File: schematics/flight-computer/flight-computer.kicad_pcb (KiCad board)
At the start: 4 copper layers, 80 x 80 mm, 114 parts, among them J101 BATT, J102 CHG, J103 Expansion Slot, J104 SWD, J105 BLACKBOX, J106 USB C, J107 GPS, J108 TELEM, J301 BMI-S-201, Q401 Si9933CDY, Q402 BSS138, U101 MAX14787E, U102 STM32F405RGT6, U201 NVT2006BQ, U202 PCA9306, U203 ICM-20789, U204 MS5611-01BA, U301 Si4463, U302 MAX-M8Q, U401 BQ29200, U402 LTC4002-ES8, U403 MAX604, U404 MAX604, Y101 26M, Y301 LFTCXO068373

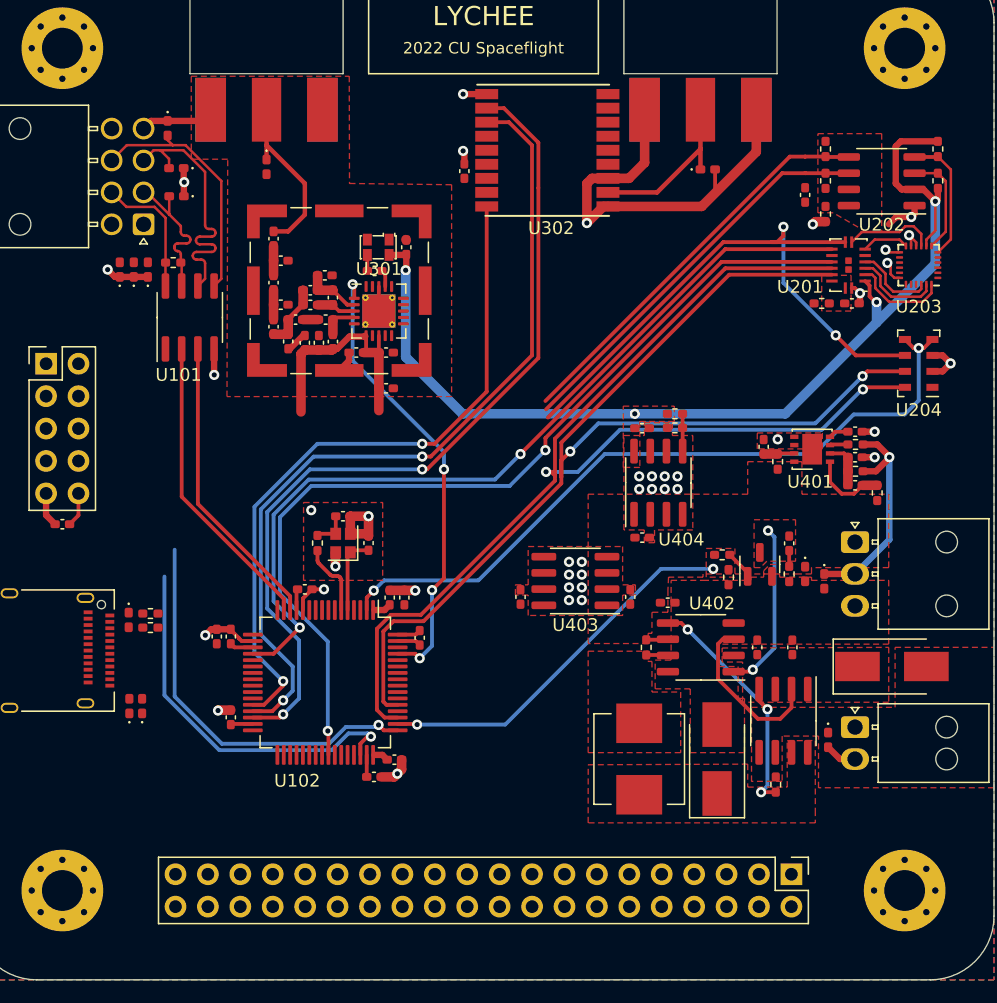
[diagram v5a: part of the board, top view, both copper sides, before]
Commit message: Change peripheral interface assignments to match layout
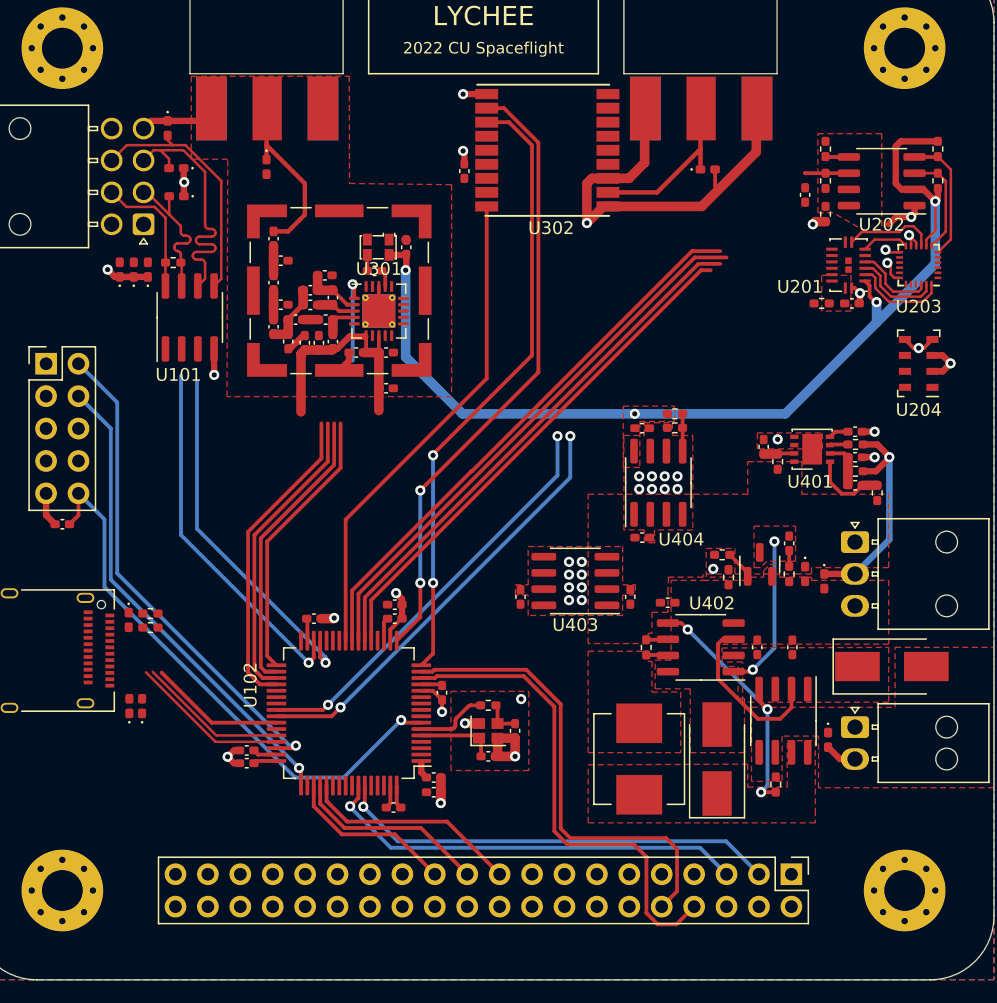
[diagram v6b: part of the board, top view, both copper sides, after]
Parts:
- moved J107 34.1 mm to (225.8, 109.8)
- moved J108 34.0 mm to (191.8, 109.8)
- moved C104 21.6 mm to (211.2, 158.6), turned to 90 degrees
- moved C103 19.2 mm to (209.1, 160.6), turned to 180 degrees
- moved Y101 18.6 mm to (209.1, 158.6), turned to 0 degrees
- moved R102 18.5 mm to (209.1, 156.6), turned to 180 degrees
- moved C106 15.4 mm to (204.8, 163.4), turned to 180 degrees
- moved C105 14.5 mm to (204.8, 162.2), turned to 180 degrees
- moved C108 14.2 mm to (201.8, 148.7), turned to 180 degrees
- moved C107 13.5 mm to (205.4, 155.6), turned to 90 degrees
- moved C112 13.5 mm to (201.7, 164.6), turned to 0 degrees
- moved C101 12.9 mm to (201.8, 149.8), turned to 180 degrees
- moved C102 11.6 mm to (190.2, 161.1), turned to 0 degrees
- moved C110 10.2 mm to (190.2, 160.1), turned to 0 degrees
- moved C109 10.1 mm to (195.4, 149.8), turned to 180 degrees
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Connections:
- J103 pad 10: /EXT_RX -> /UART4_RX
- J103 pad 19: /SPI1_MOSI -> /SPI3_MOSI
- J103 pad 21: /SPI1_MISO -> /SPI3_MISO
- J103 pad 23: /SPI1_SCLK -> /SPI3_SCLK
- J103 pad 3: /EXT_SDA -> /I2C1_SDA
- J103 pad 5: /EXT_SCL -> /I2C1_SCL
- J103 pad 8: /EXT_TX -> /UART4_TX
- R201 pad 2: /IMU_PR_CL -> /I2C3_SCL
- R202 pad 2: /IMU_PR_DA -> /I2C3_SDA
- U101 pad 2: /UART4_RX -> /USART3_RX
- U101 pad 3: /UART4_TX -> /USART3_TX
- U102 pad 16: unconnected-(U102-Pad16) -> /USART2_TX
- U102 pad 17: unconnected-(U102-Pad17) -> /USART2_RX
- U102 pad 20: /IMU_INT -> unconnected-(U102-Pad20)
- U102 pad 24: unconnected-(U102-Pad24) -> /IMU_INT
- U102 pad 25: unconnected-(U102-Pad25) -> /GPS_~{RESET}
- U102 pad 28: /GPS_~{RESET} -> unconnected-(U102-Pad28)
- U102 pad 40: unconnected-(U102-Pad40) -> /I2C3_SDA
- U102 pad 41: /IMU_~{CS} -> /I2C3_SCL
- U102 pad 43: unconnected-(U102-Pad43) -> /IMU_~{CS}
- U102 pad 58: /IMU_PR_CL -> /I2C1_SCL
- U102 pad 59: /IMU_PR_DA -> /I2C1_SDA
- U201 pad 13: /SPI3_SCLK -> /SPI1_SCLK
- U201 pad 14: /SPI3_MOSI -> /SPI1_MOSI
- U201 pad 9: /SPI3_MISO -> /SPI1_MISO
- U202 pad 5: /IMU_PR_DA -> /I2C3_SDA
- U202 pad 6: /IMU_PR_CL -> /I2C3_SCL
- U204 pad 6: /SPI3_MISO -> /SPI1_MISO
- U204 pad 7: /SPI3_MOSI -> /SPI1_MOSI
- U204 pad 8: /SPI3_SCLK -> /SPI1_SCLK
- U302 pad 2: /USART3_RX -> /USART2_RX
- U302 pad 3: /USART3_TX -> /USART2_TX
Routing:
- net /SPI3_SCLK: track 89.2 -> 13.3 mm, vias 2 -> 0
- net /IMU_~{CS}: track 72.3 -> 0.00 mm, vias 2 -> 0
- net /SPI3_MOSI: track 86.4 -> 17.2 mm, vias 2 -> 0
- net /BARO_~{CS}: track 57.4 -> 2.71 mm, vias 2 -> 1
- net /USART2_RX: track 0.00 -> 48.8 mm, vias 0 -> 2
- net /USART2_TX: track 0.00 -> 48.6 mm, vias 0 -> 2
- net /SPI1_MOSI: track 0.00 -> 43.4 mm
- net /SPI1_MISO: track 0.00 -> 42.1 mm
- net /NRST: track 2.70 -> 43.8 mm, vias 0 -> 1
- net /SPI1_SCLK: track 0.00 -> 40.5 mm
- net /USART3_RX: track 68.2 -> 28.5 mm, vias 2 -> 1
- net /USART3_TX: track 66.0 -> 28.1 mm, vias 2 -> 1
- net /I2C3_SCL: track 0.00 -> 37.4 mm, vias 0 -> 2
- net /I2C1_SDA: track 0.00 -> 34.9 mm, vias 0 -> 1
- net /I2C3_SDA: track 0.00 -> 34.5 mm, vias 0 -> 2
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
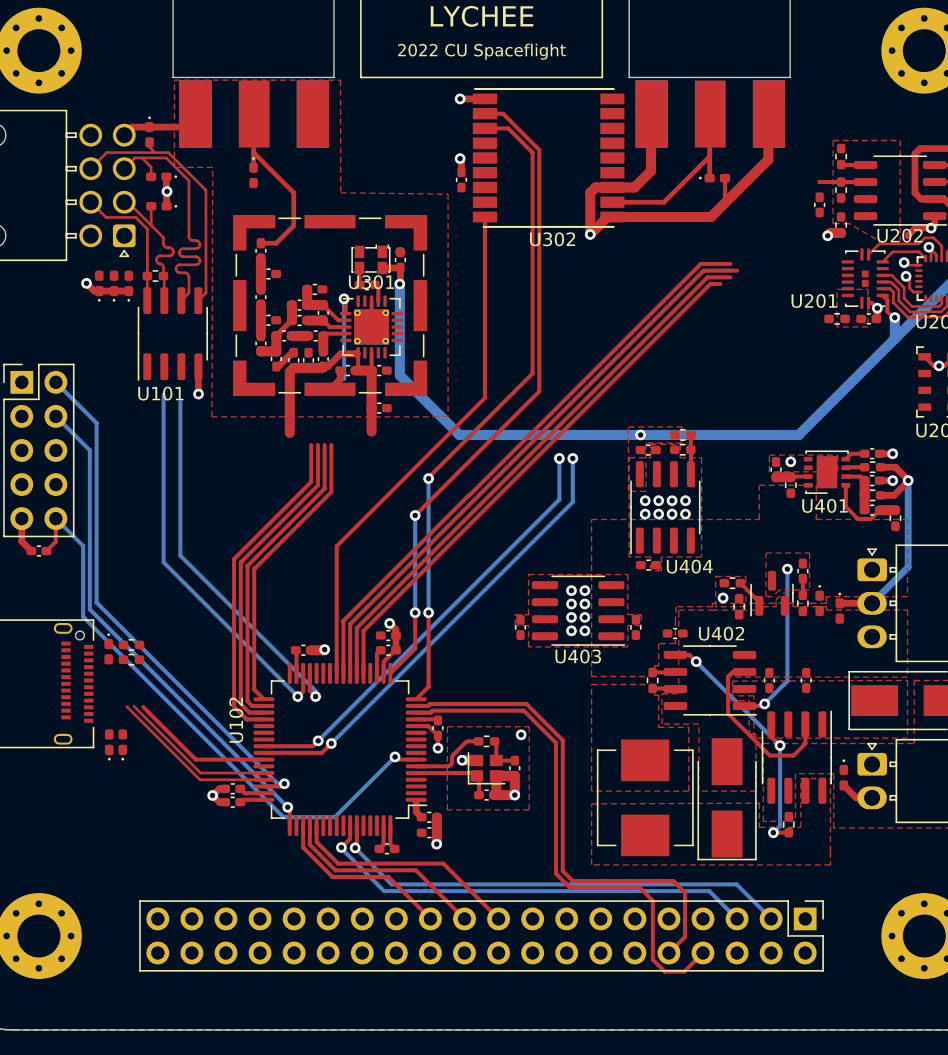
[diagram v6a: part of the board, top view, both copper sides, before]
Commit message: Route GPIO peripheral connections
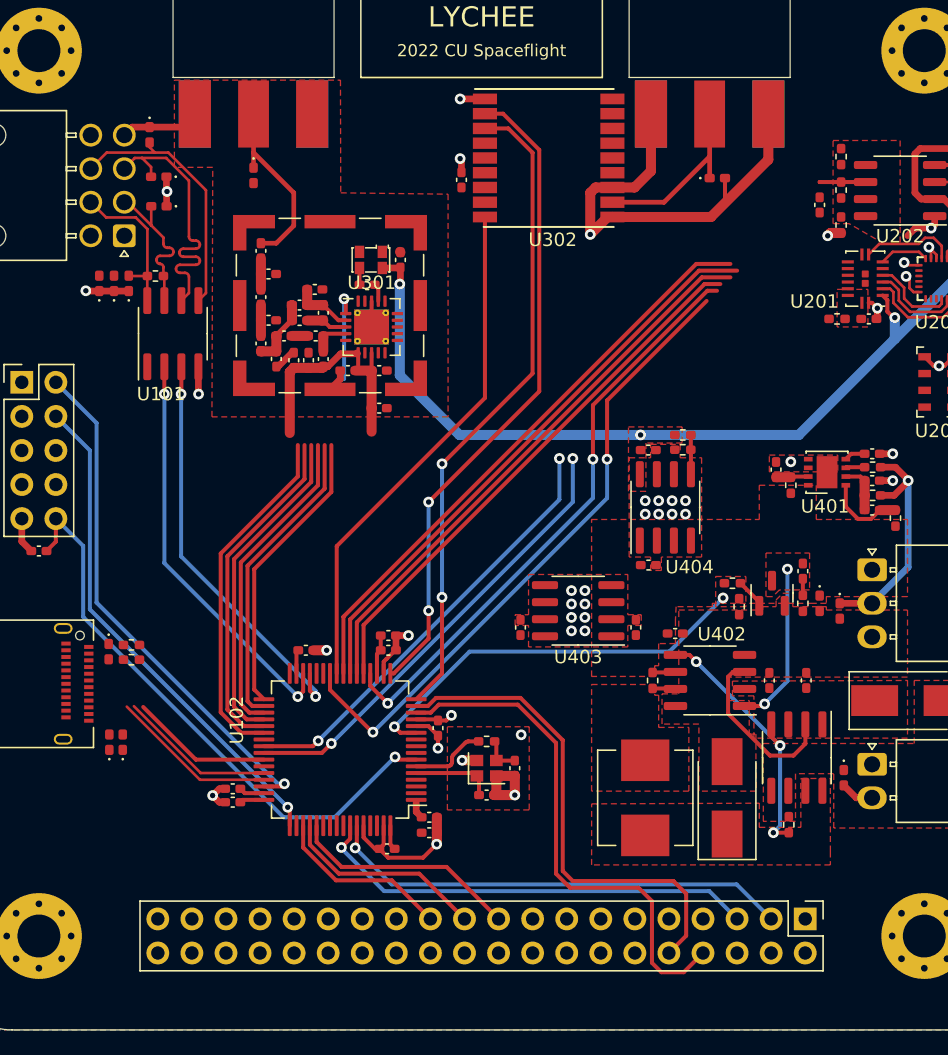
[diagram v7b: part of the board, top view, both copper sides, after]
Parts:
- moved C109 0.18 mm to (195.6, 149.8)
- moved J107 0.05 mm to (225.7, 109.8)
- moved J108 0.05 mm to (191.7, 109.8)
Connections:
- U102 pad 11: unconnected-(U102-Pad11) -> /CHG_SDN
- U102 pad 2: /BARO_~{CS} -> unconnected-(U102-Pad2)
- U102 pad 20: unconnected-(U102-Pad20) -> /BARO_~{CS}
- U102 pad 26: unconnected-(U102-Pad26) -> /IMU_~{CS}
- U102 pad 37: unconnected-(U102-Pad37) -> /RADIO_~{INT}
- U102 pad 38: unconnected-(U102-Pad38) -> /RADIO_SDN
- U102 pad 43: /IMU_~{CS} -> unconnected-(U102-Pad43)
- U102 pad 50: /CHG_SDN -> unconnected-(U102-Pad50)
- U102 pad 61: /RADIO_SDN -> unconnected-(U102-Pad61)
- U102 pad 62: /RADIO_~{INT} -> unconnected-(U102-Pad62)
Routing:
- net /IMU_~{CS}: track 0.00 -> 48.2 mm, vias 0 -> 2
- net /BARO_~{CS}: track 2.71 -> 46.8 mm, vias 1 -> 3
- net /CHG_SDN: track 0.00 -> 30.3 mm, vias 1 -> 2
- net /RADIO_SDN: track 7.14 -> 33.3 mm
- net /RADIO_~{INT}: track 0.00 -> 25.3 mm
- net GND: track 96.6 -> 103.6 mm
- net /USART3_TX: track 28.1 -> 30.6 mm, vias 1 -> 2
- net 3v3: track 29.5 -> 31.8 mm, vias 2 -> 3
- net /USART3_RX: track 28.5 -> 30.6 mm, vias 1 -> 2
- net /I2C3_SDA: track 34.5 -> 32.7 mm
- net /BB_RX+: track 10.4 -> 11.8 mm
- net /UART4_TX: track 38.4 -> 38.9 mm
